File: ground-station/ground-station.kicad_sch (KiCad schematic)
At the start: 15 parts

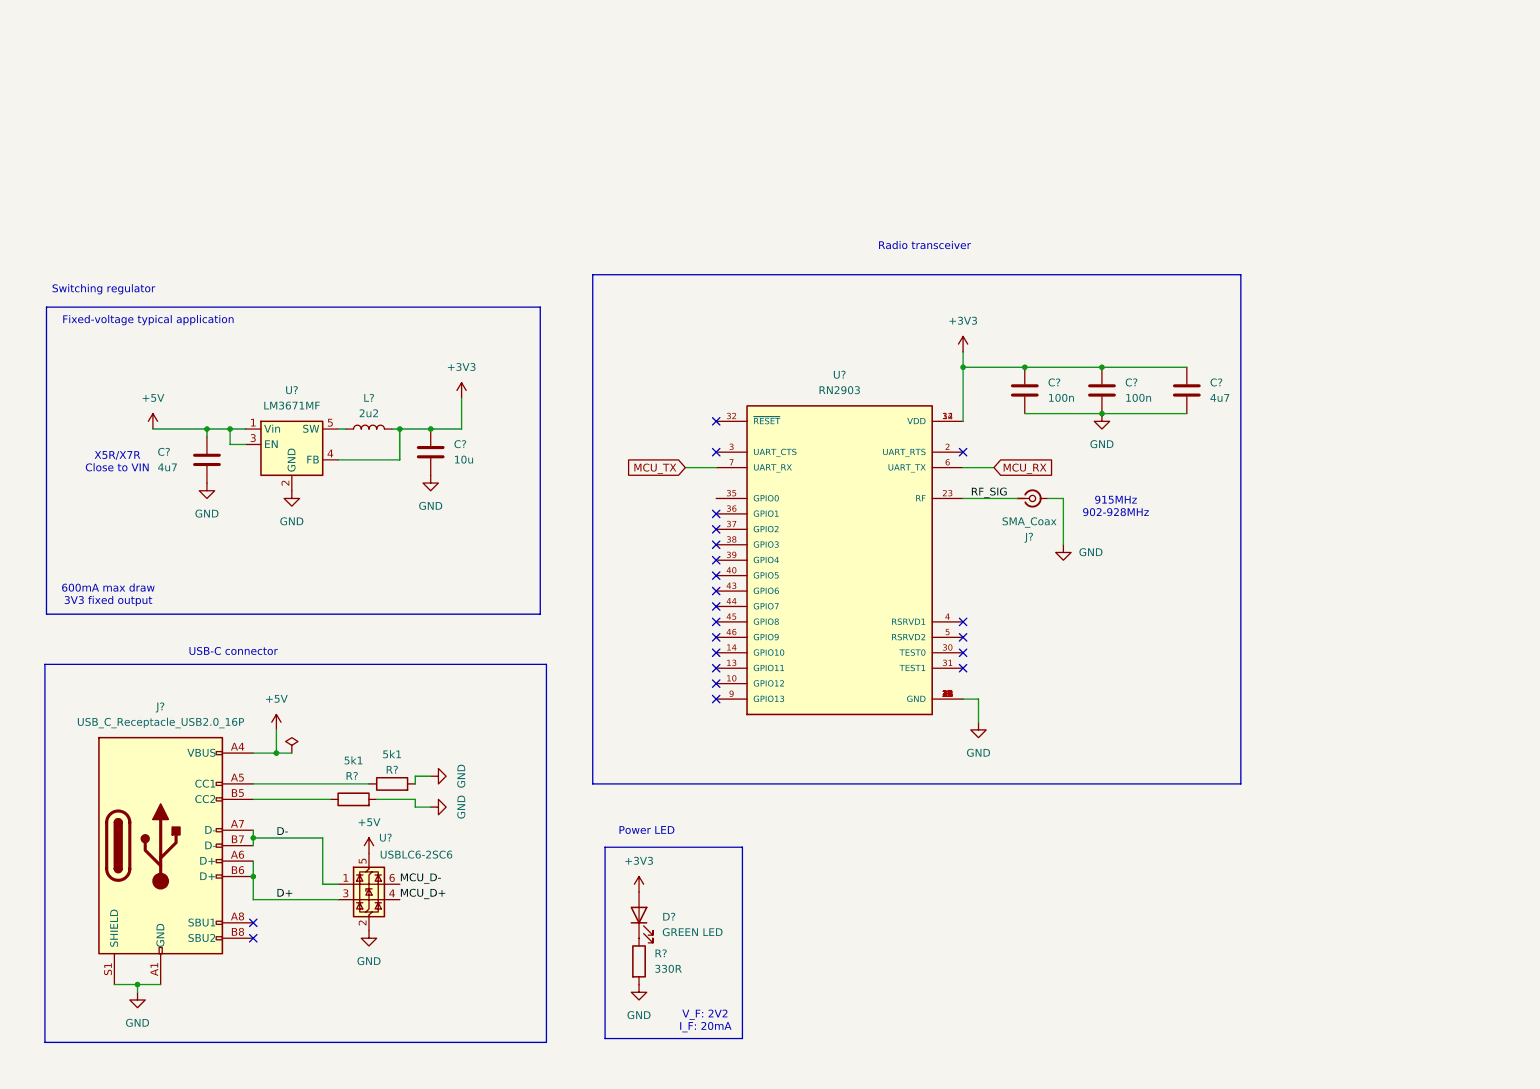
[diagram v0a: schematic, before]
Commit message: Removed DRC errors on schematic by adding power flags.
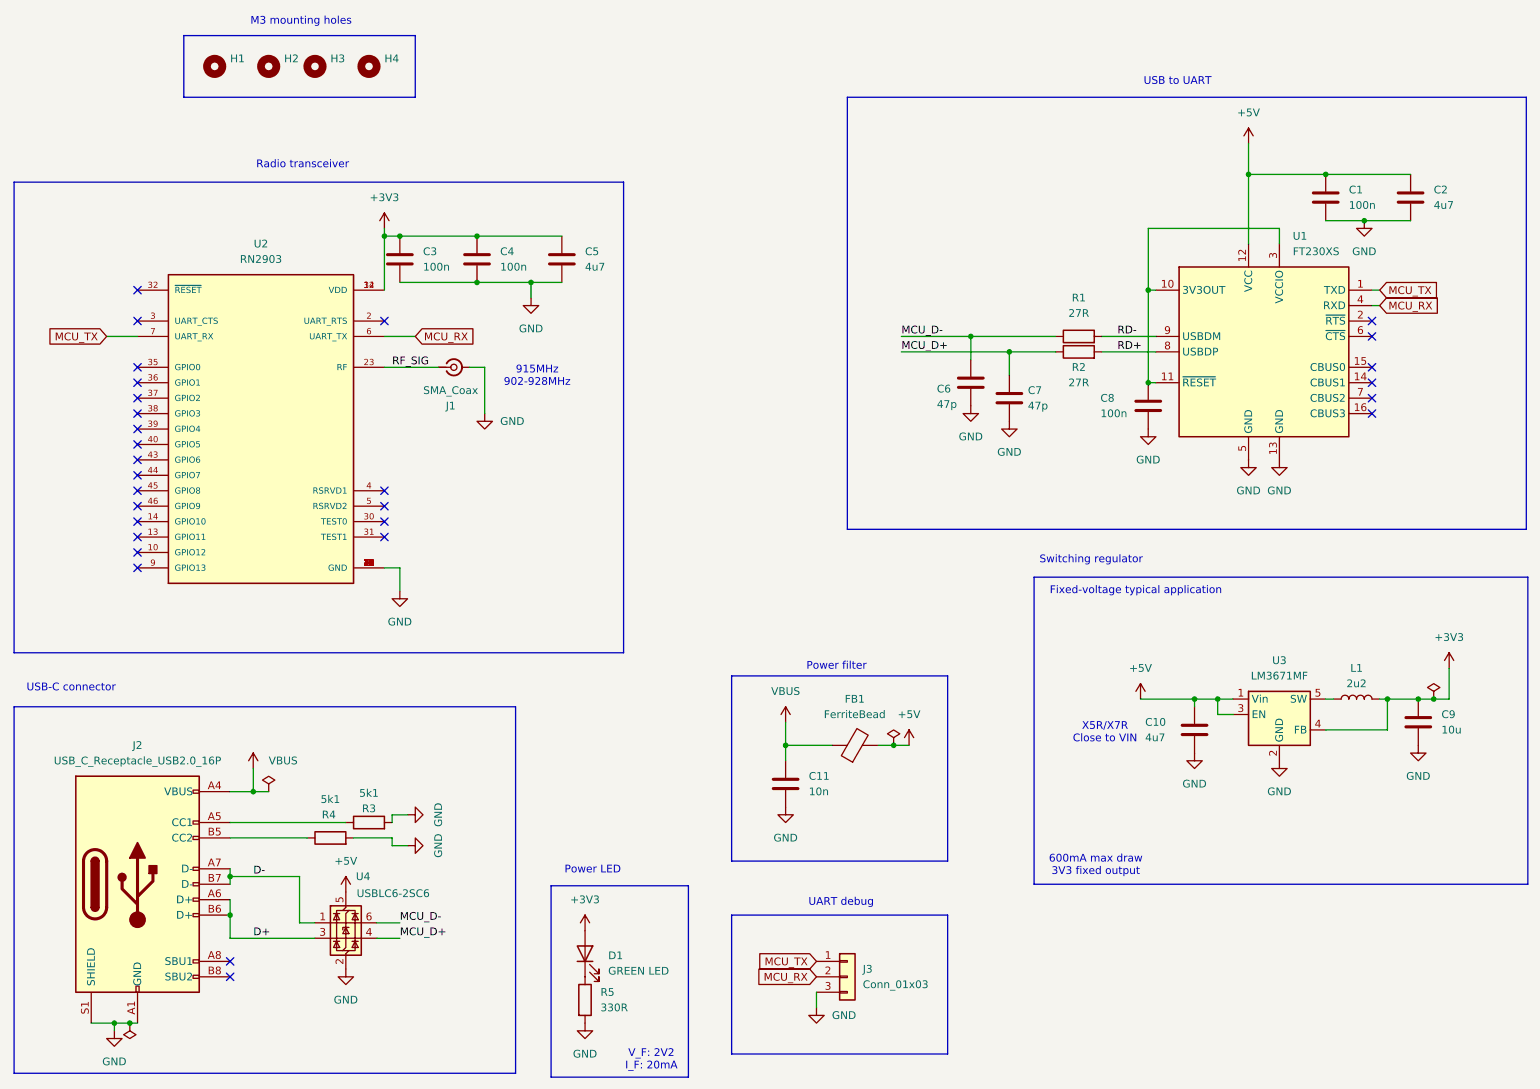
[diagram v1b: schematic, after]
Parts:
- added C1, C8: 100n, Capacitor_SMD:C_0402_1005Metric, symbol Device:C
- added C11: 10n, symbol Device:C
- added C2: 4u7, Capacitor_SMD:C_0603_1608Metric, symbol Device:C
- added C6, C7: 47p, symbol Device:C
- added FB1: FerriteBead, symbol Device:FerriteBead
- added H1, H2, H3, H4: MountingHole, MountingHole:MountingHole_3.2mm_M3, symbol Mechanical:MountingHole
- added J3: Conn_01x03, symbol Connector_Generic:Conn_01x03
- added R1, R2: 27R, Resistor_SMD:R_0402_1005Metric, symbol Device:R
- added U1: FT230XS, Package_SO:SSOP-16_3.9x4.9mm_P0.635mm, symbol Interface_USB:FT230XS
- gave numbers to parts that had none: 15
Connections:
- net +5V: now also C1.1, C2.1, FB1.2, U1.12 (VCC); no longer J2.A4 (VBUS), J2.A9 (VBUS), J2.B4 (VBUS), J2.B9 (VBUS)
- net GND: now also C1.2, C11.2, C2.2, C6.2, C7.2, C8.2, J3.3 (Pin_3), U1.13 (GND), U1.5 (GND)
- net MCU_D+: now also C7.1, R2.1
- net MCU_D-: now also C6.1, R1.1
- net MCU_RX: now also J3.2 (Pin_2), U1.4 (RXD)
- net MCU_TX: now also J3.1 (Pin_1), U1.1 (TXD)
- new net: C8.1, U1.10 (3V3OUT), U1.11 (~{RESET}), U1.3 (VCCIO)
- new net RD+: R2.2, U1.8 (USBDP)
- new net RD-: R1.2, U1.9 (USBDM)
- new net VBUS: C11.1, FB1.1, J2.A4 (VBUS), J2.A9 (VBUS), J2.B4 (VBUS), J2.B9 (VBUS)
- no-connect marks 22 -> 29
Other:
- note added: "M3 mounting holes"
- note added: "Power filter"
- note added: "UART debug"
- note added: "USB to UART"
- moved on the sheet: C10, C3, C4, C5, C9, D1, J1, J2, L1, R3, R4, R5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

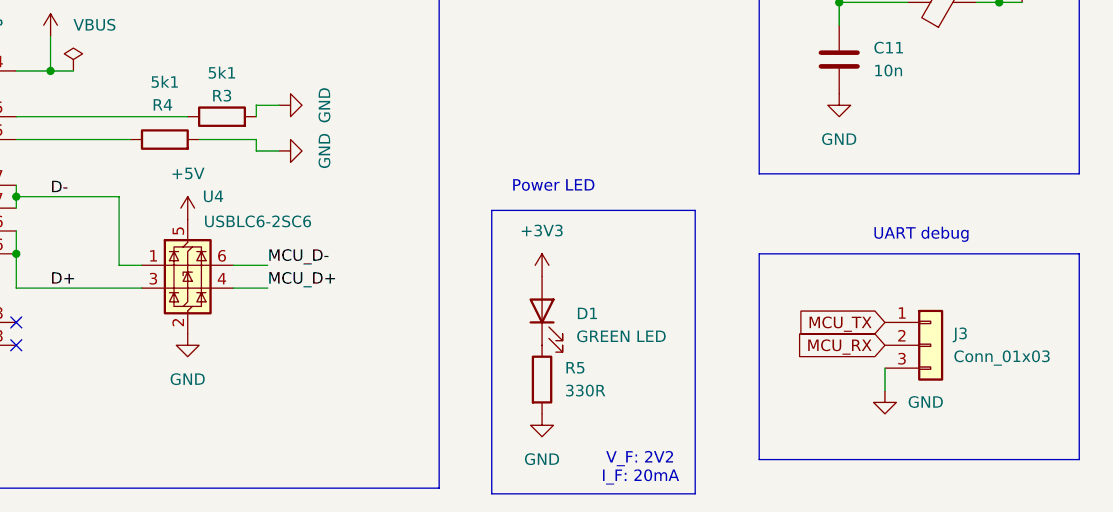
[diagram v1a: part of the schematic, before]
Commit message: Created initial PCB layout for ground station.
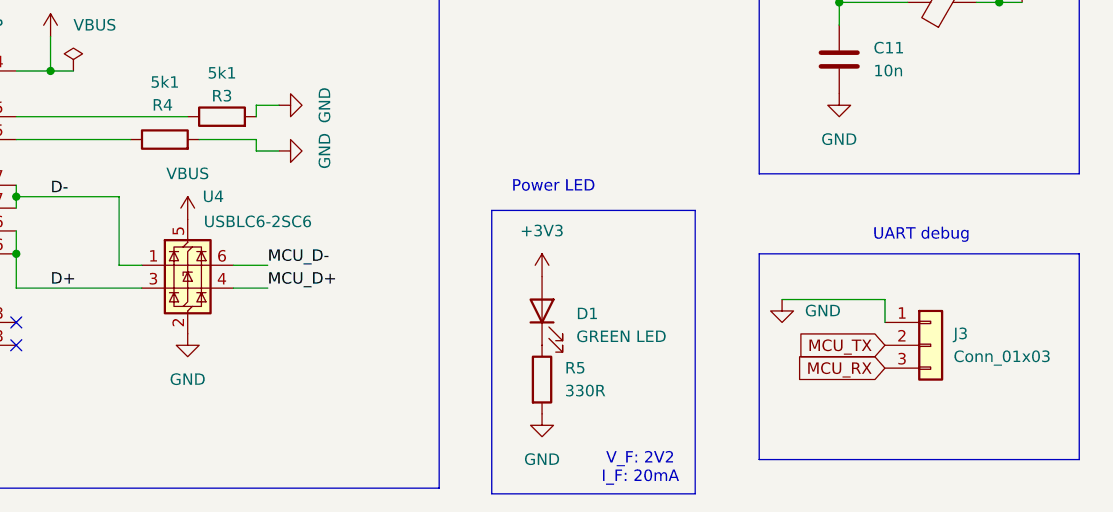
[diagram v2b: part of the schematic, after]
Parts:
- C11: footprint (none) -> Capacitor_SMD:C_0402_1005Metric; MP (none) -> KAM05AR71E103KH
- C6, C7: footprint (none) -> Capacitor_SMD:C_0402_1005Metric; MP (none) -> C0402C470K3RACAUTO
- FB1: footprint (none) -> Inductor_SMD:L_0805_2012Metric; MP (none) -> MI0805K601R-10
- J3: footprint (none) -> Connector_PinHeader_2.54mm:PinHeader_1x03_P2.54mm_Vertical; MP (none) -> 78511-203HLF
- U1: MP (none) -> FT230XS-R
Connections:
- net +5V: no longer U4.5 (VBUS)
- net GND: now also J3.1 (Pin_1); no longer J3.3 (Pin_3)
- net MCU_RX: now also J3.3 (Pin_3); no longer J3.2 (Pin_2)
- net MCU_TX: now also J3.2 (Pin_2); no longer J3.1 (Pin_1)
- net VBUS: now also U4.5 (VBUS)
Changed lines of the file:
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@@
 	(wire
 		(pts
+			(xy 147.32 172.72) (xy 135.89 172.72)
+		)
+		(stroke
+			(width 0)
+			(type default)
+		)
+	)
+	(wire
+		(pts
 			(xy 77.47 156.21) (xy 77.47 154.94)
 		)
@@
 	(wire
 		(pts
+			(xy 147.32 175.26) (xy 147.32 172.72)
+		)
+		(stroke
+			(width 0)
+			(type default)
+		)
+	)
+	(wire
+		(pts
 			(xy 62.23 168.91) (xy 64.77 168.91)
 		)
@@
 	(wire
 		(pts
-			(xy 147.32 182.88) (xy 147.32 180.34)
-		)
-		(stroke
-			(width 0)
-			(type default)
-		)
-	)
-	(wire
-		(pts
 			(xy 77.47 154.94) (xy 71.12 154.94)
 		)
@@
 		)
 	)
-	(global_label "MCU_TX"
+	(global_label "MCU_RX"
 		(shape input)
-		(at 240.03 64.77 0)
+		(at 147.32 180.34 180)
 		(fields_autoplaced yes)
 		(effects
@@
 				(size 1.27 1.27)
 			)
-			(justify left)
+			(justify right)
 		)
 		(property "Intersheetrefs" "${INTERSHEET_REFS}"
-			(at 250.2118 64.77 0)
+			(at 136.8358 180.34 0)
 			(effects
 				(font
 					(size 1.27 1.27)
 				)
-				(justify left)
+				(justify right)
 				(hide yes)
 			)
@@
 	(global_label "MCU_TX"
 		(shape input)
-		(at 147.32 175.26 180)
+		(at 240.03 64.77 0)
 		(fields_autoplaced yes)
 		(effects
@@
 				(size 1.27 1.27)
 			)
-			(justify right)
+			(justify left)
 		)
 		(property "Intersheetrefs" "${INTERSHEET_REFS}"
-			(at 137.1382 175.26 0)
+			(at 250.2118 64.77 0)
 			(effects
 				(font
 					(size 1.27 1.27)
 				)
-				(justify right)
+				(justify left)
 				(hide yes)
 			)
@@
 	(global_label "MCU_TX"
 		(shape input)
-		(at 30.48 72.39 180)
+		(at 147.32 177.8 180)
 		(fields_autoplaced yes)
 		(effects
@@
 		)
 		(property "Intersheetrefs" "${INTERSHEET_REFS}"
-			(at 20.2982 72.39 0)
+			(at 137.1382 177.8 0)
 			(effects
 				(font
@@
 		)
 	)
-	(global_label "MCU_RX"
+	(global_label "MCU_TX"
 		(shape input)
-		(at 147.32 177.8 180)
+		(at 30.48 72.39 180)
 		(fields_autoplaced yes)
 		(effects
@@
 		)
 		(property "Intersheetrefs" "${INTERSHEET_REFS}"
-			(at 136.8358 177.8 0)
+			(at 20.2982 72.39 0)
 			(effects
 				(font
@@
 			)
 		)
-		(property "Value" "+5V"
+		(property "Value" "VBUS"
 			(at 69.85 158.75 0)
 			(effects
@@
 			)
 		)
-		(property "Footprint" ""
+		(property "Footprint" "Capacitor_SMD:C_0402_1005Metric"
 			(at 173.6852 83.82 0)
 			(effects
@@
 			)
 		)
+		(property "MP" "C0402C470K3RACAUTO"
+			(at 172.72 80.01 0)
+			(effects
+				(font
+					(size 1.27 1.27)
+				)
+				(hide yes)
+			)
+		)
 		(pin "2"
 		)
@@
 			)
 		)
-		(property "Footprint" ""
+		(property "Footprint" "Connector_PinHeader_2.54mm:PinHeader_1x03_P2.54mm_Vertical"
 			(at 152.4 177.8 0)
 			(effects
@@
 			)
 		)
-		(property "Datasheet" "~"
+		(property "Datasheet" "https://www.mouser.ca/datasheet/2/18/68000-1266375.pdf"
 			(at 152.4 177.8 0)
 			(effects
@@
 			)
 		)
+		(property "MP" "78511-203HLF"
+			(at 152.4 177.8 0)
+			(effects
+				(font
+					(size 1.27 1.27)
+				)
+				(hide yes)
+			)
+		)
 		(pin "1"
 		)
@@
 	(symbol
 		(lib_id "power:GND")
-		(at 147.32 182.88 0)
+		(at 135.89 172.72 0)
 		(unit 1)
 		(exclude_from_sim no)
@@
 		(fields_autoplaced yes)
 		(property "Reference" "#PWR015"
-			(at 147.32 189.23 0)
+			(at 135.89 179.07 0)
 			(effects
 				(font
@@
 		)
 		(property "Value" "GND"
-			(at 149.86 184.1499 0)
+			(at 138.43 173.9899 0)
 			(effects
 				(font
@@
 		)
 		(property "Footprint" ""
-			(at 147.32 182.88 0)
+			(at 135.89 172.72 0)
 			(effects
 				(font
@@
 		)
 		(property "Datasheet" ""
-			(at 147.32 182.88 0)
+			(at 135.89 172.72 0)
 			(effects
 				(font
@@
 		)
 		(property "Description" "Power symbol creates a global label with name \"GND\" , ground"
-			(at 147.32 182.88 0)
+			(at 135.89 172.72 0)
 			(effects
 				(font
@@
 			)
 		)
+		(property "MP" "FT230XS-R"
+			(at 220.98 74.93 0)
+			(effects
+				(font
+					(size 1.27 1.27)
+				)
+				(hide yes)
+			)
+		)
 		(pin "9"
 		)
@@
 			)
 		)
-		(property "Datasheet" "https://product.tdk.com/system/files/dam/doc/product/capacitor/ceramic/mlcc/catalog/mlcc_automotive_general_en.pdf?ref_disty=mouser"
+		(property "Datasheet" "https://www.mouser.ca/datasheet/2/447/KEM_C1023_X7R_AUTO_SMD-3316698.pdf"
 			(at 209.55 137.16 0)
 			(effects
@@
 			)
 		)
-		(property "Footprint" ""
+		(property "Footprint" "Capacitor_SMD:C_0402_1005Metric"
 			(at 143.2052 149.86 0)
 			(effects
@@
 			)
 		)
-		(property "Datasheet" "~"
+		(property "Datasheet" "https://www.mouser.ca/datasheet/2/40/AutoMLCCKAM-3216307.pdf"
 			(at 142.24 146.05 0)
 			(effects
@@
 			)
 		)
+		(property "MP" "KAM05AR71E103KH"
+			(at 142.24 146.05 0)
+			(effects
+				(font
+					(size 1.27 1.27)
+				)
+				(hide yes)
+			)
+		)
 		(pin "2"
 		)
@@
 			)
 		)
-		(property "Datasheet" "https://product.tdk.com/system/files/dam/doc/product/capacitor/ceramic/mlcc/catalog/mlcc_automotive_general_en.pdf?ref_disty=mouser"
+		(property "Datasheet" "https://www.mouser.ca/datasheet/2/447/KEM_C1023_X7R_AUTO_SMD-3316698.pdf"
 			(at 105.41 59.69 0)
 			(effects
@@
 			)
 		)
-		(property "Datasheet" "https://product.tdk.com/system/files/dam/doc/product/capacitor/ceramic/mlcc/catalog/mlcc_automotive_general_en.pdf?ref_disty=mouser"
+		(property "Datasheet" "https://www.mouser.ca/datasheet/2/447/KEM_C1023_X7R_AUTO_SMD-3316698.pdf"
 			(at 245.11 49.53 0)
 			(effects
@@
 			)
 		)
-		(property "Footprint" ""
+		(property "Footprint" "Capacitor_SMD:C_0402_1005Metric"
 			(at 180.0352 86.36 0)
 			(effects
@@
 			)
 		)
+		(property "MP" "C0402C470K3RACAUTO "
+			(at 179.07 82.55 0)
+			(effects
+				(font
+					(size 1.27 1.27)
+				)
+				(hide yes)
+			)
+		)
 		(pin "2"
 		)
@@
 			)
 		)
-		(property "Footprint" ""
+		(property "Footprint" "Inductor_SMD:L_0805_2012Metric"
 			(at 153.67 141.478 90)
 			(effects
@@
 			)
 		)
-		(property "Datasheet" "~"
+		(property "Datasheet" "https://www.mouser.ca/datasheet/2/987/mi0805k601r_10_datasheet-2947150.pdf"
 			(at 153.67 139.7 0)
 			(effects
@@
 			(at 153.67 139.7 0)
 			(effects
+				(font
+					(size 1.27 1.27)
+				)
+				(hide yes)
+			)
+		)
+		(property "MP" "MI0805K601R-10"
+			(at 153.67 139.7 0)
+			(effects

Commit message: Routing finished for ground station.
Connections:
- net PWR_NSY: now reaches L1.1, U3.5 (SW)
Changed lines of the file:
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@@
+	)
+	(junction
+		(at 231.14 132.08)
+		(diameter 0)
+		(color 0 0 0 0)
 	)
 	(junction
@@
 		(pts
 			(xy 80.01 151.13) (xy 77.47 151.13)
+		)
+		(stroke
+			(width 0)
+			(type default)
+		)
+	)
+	(wire
+		(pts
+			(xy 231.14 125.73) (xy 231.14 132.08)
 		)
 		(stroke
@@
 		)
 	)
+	(label "PWR_NSY"
+		(at 231.14 125.73 0)
+		(fields_autoplaced yes)
+		(effects
+			(font
+				(size 1.27 1.27)
+			)
+			(justify left bottom)
+		)
+	)

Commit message: BOMS exported and sorted.
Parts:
- C7: MP C0402C470K3RACAUTO -> C0402C470K3RACAUTO
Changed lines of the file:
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@@
 			)
 		)
-		(property "MP" "C0402C470K3RACAUTO "
+		(property "MP" "C0402C470K3RACAUTO"
 			(at 179.07 82.55 0)
 			(effects

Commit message: Remove out of stock LED from BOMS
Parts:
- D1: MP LG R971-KN-1 -> HSMG-C170
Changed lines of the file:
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@@
 			)
 		)
-		(property "Datasheet" "https://www.mouser.ca/datasheet/2/588/prd_pim_datasheet_2191277_EN_pdf-3419125.pdf"
+		(property "Datasheet" ""
 			(at 109.22 173.99 0)
 			(effects
@@
 			)
 		)
-		(property "MP" "LG R971-KN-1"
+		(property "MP" "HSMG-C170"
 			(at 109.22 173.99 0)
 			(effects
